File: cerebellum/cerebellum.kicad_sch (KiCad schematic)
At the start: 25 parts, among them J1 GPIO, J2 Conn_MOTA, J3 Conn_MOTB, J4 MD_POW, J5 Conn_SPI, J6 Conn_UART, J7 Conn_I2C, J8 VBUS(OUT), J9 3V3(OUT), SW1 SW_PULLUP, SW2 SW_PULLDOWN, SW3 SW_SPDT, U2 POLOLU_TB6612_CARRIER, U3 HC-SR04

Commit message: update design
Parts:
- SW1: value SW_PULLUP -> PULLUP
- SW2: value SW_PULLDOWN -> PULLDOWN
- SW3: footprint Button_Switch_THT:SW_E-Switch_EG1271_SPDT -> Connector_PinHeader_2.54mm:PinHeader_1x03_P2.54mm_Vertical
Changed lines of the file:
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@@
 			)
 		)
-		(property "Value" "SW_PULLUP"
+		(property "Value" "PULLUP"
 			(at 93.218 129.54 0)
 			(effects
@@
 			)
 		)
-		(property "Value" "SW_PULLDOWN"
+		(property "Value" "PULLDOWN"
 			(at 119.888 120.65 0)
 			(effects
@@
 			)
 		)
-		(property "Footprint" "Button_Switch_THT:SW_E-Switch_EG1271_SPDT"
+		(property "Footprint" "Connector_PinHeader_2.54mm:PinHeader_1x03_P2.54mm_Vertical"
 			(at 106.68 29.21 0)
 			(effects

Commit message: organize schematic
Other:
- note added: "Motor Driver"
- note added: "Pico & Peripherals"
- note added: "Pin Headers"
- title: RPi Expansion for Pico and Motor Driver (The Cerebellum) -> R1R Cerebellum
- moved on the sheet: A1, C2, C3, D1, J1, J2, J3, J4, J5, J6, J7, J8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

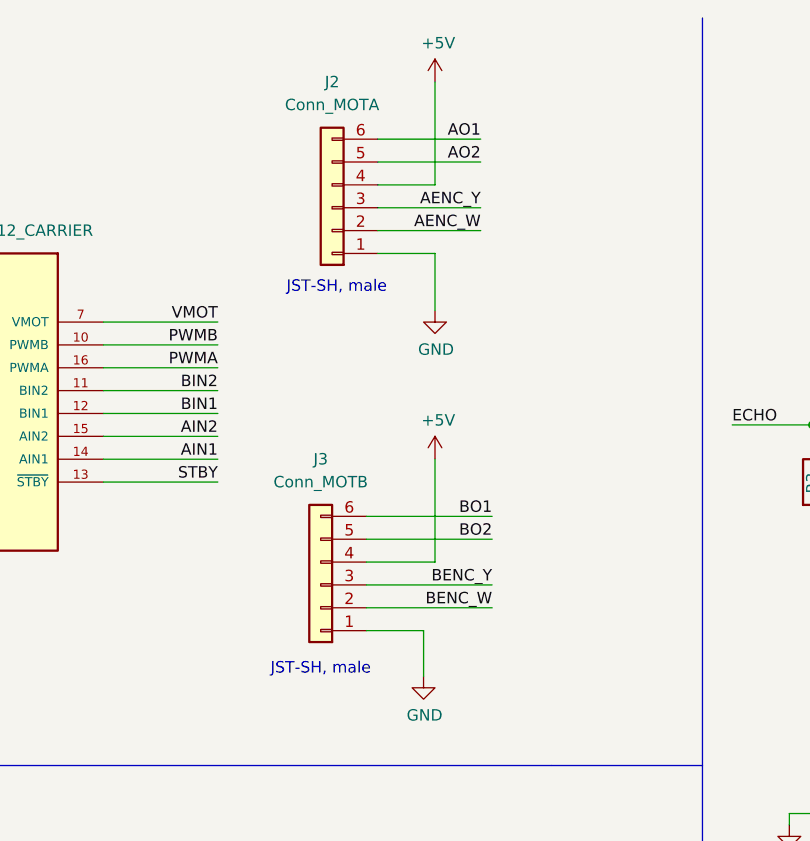
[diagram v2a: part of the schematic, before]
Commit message: update motor connector in schematic
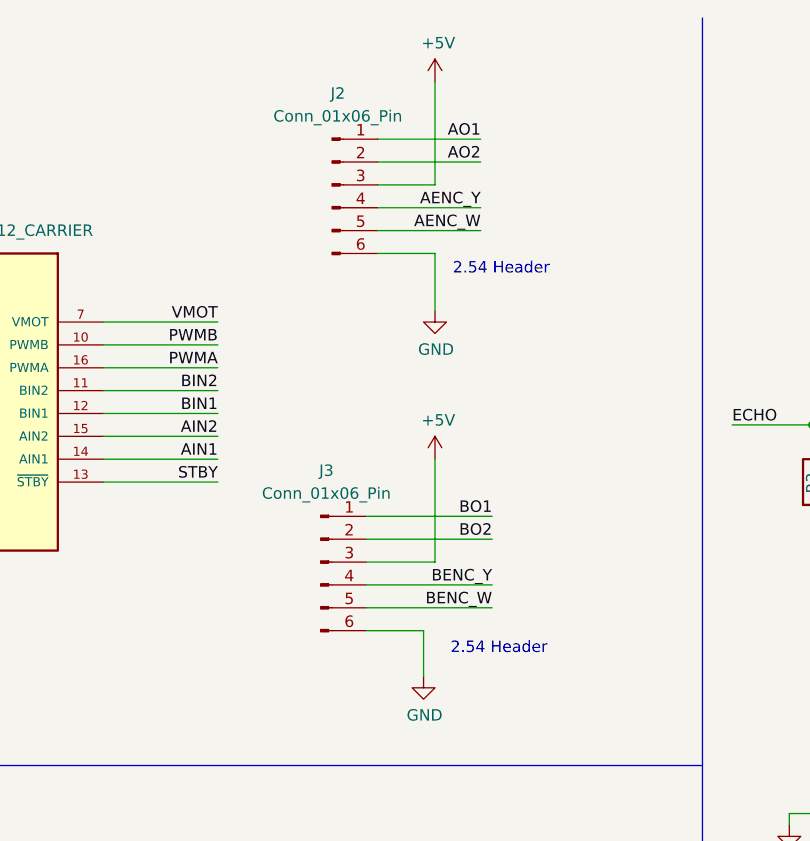
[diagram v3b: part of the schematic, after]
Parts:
- removed J2: Conn_MOTA, Connector_JST:JST_SH_BM06B-SRSS-TB_1x06-1MP_P1.00mm_Vertical, symbol Connector_Generic:Conn_01x06
- removed J3: Conn_MOTB, Connector_JST:JST_SH_BM06B-SRSS-TB_1x06-1MP_P1.00mm_Vertical, symbol Connector_Generic:Conn_01x06
- added J2, J3: Conn_01x06_Pin, Connector_PinHeader_2.54mm:PinHeader_1x06_P2.54mm_Vertical, symbol Connector:Conn_01x06_Pin
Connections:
- net +5V: now also J2.3 (Pin_3), J3.3 (Pin_3)
- net AENC_W: now also J2.5 (Pin_5)
- net AENC_Y: now also J2.4 (Pin_4)
- net AO1: now also J2.1 (Pin_1)
- net AO2: now also J2.2 (Pin_2)
- net BENC_W: now also J3.5 (Pin_5)
- net BENC_Y: now also J3.4 (Pin_4)
- net BO1: now also J3.1 (Pin_1)
- net BO2: now also J3.2 (Pin_2)
- net GND: now also J2.6 (Pin_6), J3.6 (Pin_6)
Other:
- note removed: "JST-SH, male"
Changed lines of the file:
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@@
 		(rev "0.1")
 	)
-	(text "JST-SH, male"
+	(text "2.54 Header"
 		(exclude_from_sim no)
-		(at 90.678 41.91 0)
+		(at 108.712 82.042 0)
 		(effects
 			(font
@@
 		)
 	)
+	(text "2.54 Header"
+		(exclude_from_sim no)
+		(at 108.966 39.878 0)
+		(effects
+			(font
+				(size 1.27 1.27)
+			)
+		)
+	)
 	(text "Additional pin functions:\nhttps://pinout.xyz/"
 		(exclude_from_sim no)
@@
 		)
 	)
-	(text "JST-SH, male"
-		(exclude_from_sim no)
-		(at 88.9 84.328 0)
-		(effects
-			(font
-				(size 1.27 1.27)
-			)
-		)
-	)
 	(text "Motor Driver"
 		(exclude_from_sim no)
@@
 	)
 	(symbol
-		(lib_id "Connector_Generic:Conn_01x06")
-		(at 88.9 74.93 180)
+		(lib_id "Connector_Generic:Conn_01x02")
+		(at 30.48 17.78 0)
 		(unit 1)
 		(exclude_from_sim no)
@@
 		(dnp no)
 		(fields_autoplaced yes)
-		(property "Reference" "J3"
-			(at 88.9 60.96 0)
+		(property "Reference" "J4"
+			(at 33.02 17.7799 0)
 			(effects
 				(font
 					(size 1.27 1.27)
 				)
+				(justify left)
 			)
 		)
-		(property "Value" "Conn_MOTB"
-			(at 88.9 63.5 0)
+		(property "Value" "MD_POW"
+			(at 33.02 20.3199 0)
 			(effects
 				(font
 					(size 1.27 1.27)
 				)
+				(justify left)
 			)
 		)
-		(property "Footprint" "Connector_JST:JST_SH_BM06B-SRSS-TB_1x06-1MP_P1.00mm_Vertical"
-			(at 88.9 74.93 0)
+		(property "Footprint" "Connector_PinHeader_2.54mm:PinHeader_1x02_P2.54mm_Horizontal"
+			(at 30.48 17.78 0)
 			(effects
 				(font
@@
 		)
 		(property "Datasheet" "~"
-			(at 88.9 74.93 0)
+			(at 30.48 17.78 0)
 			(effects
 				(font
@@
 			)
 		)
-		(property "Description" "Generic connector, single row, 01x06, script generated (kicad-library-utils/schlib/autogen/connector/)"
-			(at 88.9 74.93 0)
+		(property "Description" "Generic connector, single row, 01x02, script generated (kicad-library-utils/schlib/autogen/connector/)"
+			(at 30.48 17.78 0)
 			(effects
 				(font
@@
 			)
 		)
-		(pin "1"
-		)
-		(pin "4"
-		)
 		(pin "2"
 		)
-		(pin "3"
-		)
-		(pin "6"
-		)
-		(pin "5"
+		(pin "1"
 		)
 		(instances
 			(project ""
 				(path "/e63e39d7-6ac0-4ffd-8aa3-1841a4541b55"
-					(reference "J3")
+					(reference "J4")
 					(unit 1)
 				)
@@
 	)
 	(symbol
-		(lib_id "Connector_Generic:Conn_01x02")
-		(at 30.48 17.78 0)
+		(lib_id "Device:R")
+		(at 165.1 95.25 90)
 		(unit 1)
 		(exclude_from_sim no)
@@
 		(on_board yes)
 		(dnp no)
-		(fields_autoplaced yes)
-		(property "Reference" "J4"
-			(at 33.02 17.7799 0)
+		(property "Reference" "R5"
+			(at 165.1 95.25 90)
 			(effects
 				(font
 					(size 1.27 1.27)
 				)
-				(justify left)
 			)
 		)
-		(property "Value" "MD_POW"
-			(at 33.02 20.3199 0)
+		(property "Value" "220R"
+			(at 165.1 97.282 90)
 			(effects
 				(font
 					(size 1.27 1.27)
 				)
-				(justify left)
 			)
 		)
-		(property "Footprint" "Connector_PinHeader_2.54mm:PinHeader_1x02_P2.54mm_Horizontal"
-			(at 30.48 17.78 0)
+		(property "Footprint" "Resistor_THT:R_Axial_DIN0207_L6.3mm_D2.5mm_P10.16mm_Horizontal"
+			(at 165.1 97.028 90)
 			(effects
 				(font
@@
 		)
 		(property "Datasheet" "~"
-			(at 30.48 17.78 0)
+			(at 165.1 95.25 0)
 			(effects
 				(font
@@
 			)
 		)
-		(property "Description" "Generic connector, single row, 01x02, script generated (kicad-library-utils/schlib/autogen/connector/)"
-			(at 30.48 17.78 0)
+		(property "Description" "Resistor"
+			(at 165.1 95.25 0)
 			(effects
 				(font
@@
 			(project ""
 				(path "/e63e39d7-6ac0-4ffd-8aa3-1841a4541b55"
-					(reference "J4")
+					(reference "R5")
 					(unit 1)
 				)
@@
 	)
 	(symbol
-		(lib_id "Device:R")
-		(at 165.1 95.25 90)
+		(lib_id "Connector:Conn_01x06_Pin")
+		(at 90.17 30.48 0)
 		(unit 1)
 		(exclude_from_sim no)
@@
 		(on_board yes)
 		(dnp no)
-		(property "Reference" "R5"
-			(at 165.1 95.25 90)
+		(fields_autoplaced yes)
+		(property "Reference" "J2"
+			(at 90.805 20.32 0)
 			(effects
 				(font
@@
 			)
 		)
-		(property "Value" "220R"
-			(at 165.1 97.282 90)
+		(property "Value" "Conn_01x06_Pin"
+			(at 90.805 22.86 0)
 			(effects
 				(font
@@
 			)
 		)
-		(property "Footprint" "Resistor_THT:R_Axial_DIN0207_L6.3mm_D2.5mm_P10.16mm_Horizontal"
-			(at 165.1 97.028 90)
+		(property "Footprint" "Connector_PinHeader_2.54mm:PinHeader_1x06_P2.54mm_Vertical"
+			(at 90.17 30.48 0)
 			(effects
 				(font
@@
 		)
 		(property "Datasheet" "~"
-			(at 165.1 95.25 0)
+			(at 90.17 30.48 0)
 			(effects
 				(font
@@
 			)
 		)
-		(property "Description" "Resistor"
-			(at 165.1 95.25 0)
+		(property "Description" "Generic connector, single row, 01x06, script generated"
+			(at 90.17 30.48 0)
 			(effects
 				(font
@@
 			)
 		)
-		(pin "2"
+		(pin "5"
 		)
 		(pin "1"
 		)
+		(pin "6"
+		)
+		(pin "2"
+		)
+		(pin "4"
+		)
+		(pin "3"
+		)
 		(instances
 			(project ""
 				(path "/e63e39d7-6ac0-4ffd-8aa3-1841a4541b55"
-					(reference "R5")
+					(reference "J2")
 					(unit 1)
 				)
@@
 	)
 	(symbol
-		(lib_id "Connector_Generic:Conn_01x06")
-		(at 90.17 33.02 180)
+		(lib_id "Connector:Conn_01x06_Pin")
+		(at 88.9 72.39 0)
 		(unit 1)
 		(exclude_from_sim no)
@@
 		(dnp no)
 		(fields_autoplaced yes)
-		(property "Reference" "J2"
-			(at 90.17 19.05 0)
+		(property "Reference" "J3"
+			(at 89.535 62.23 0)
 			(effects
 				(font
@@
 			)
 		)
-		(property "Value" "Conn_MOTA"
-			(at 90.17 21.59 0)
+		(property "Value" "Conn_01x06_Pin"
+			(at 89.535 64.77 0)
 			(effects
 				(font
@@
 			)
 		)
-		(property "Footprint" "Connector_JST:JST_SH_BM06B-SRSS-TB_1x06-1MP_P1.00mm_Vertical"
-			(at 90.17 33.02 0)
+		(property "Footprint" "Connector_PinHeader_2.54mm:PinHeader_1x06_P2.54mm_Vertical"
+			(at 88.9 72.39 0)
 			(effects
 				(font
@@
 		)
 		(property "Datasheet" "~"
-			(at 90.17 33.02 0)
+			(at 88.9 72.39 0)
 			(effects
 				(font
@@
 			)
 		)
-		(property "Description" "Generic connector, single row, 01x06, script generated (kicad-library-utils/schlib/autogen/connector/)"
-			(at 90.17 33.02 0)
+		(property "Description" "Generic connector, single row, 01x06, script generated"
+			(at 88.9 72.39 0)
 			(effects
 				(font
@@
 			)
 		)
-		(pin "1"
+		(pin "2"
 		)
-		(pin "3"
+		(pin "1"
 		)
-		(pin "4"
+		(pin "6"
 		)
 		(pin "5"
 		)
-		(pin "6"
+		(pin "4"
 		)
-		(pin "2"
+		(pin "3"
 		)
 		(instances
 			(project ""
 				(path "/e63e39d7-6ac0-4ffd-8aa3-1841a4541b55"
-					(reference "J2")
+					(reference "J3")
 					(unit 1)
 				)

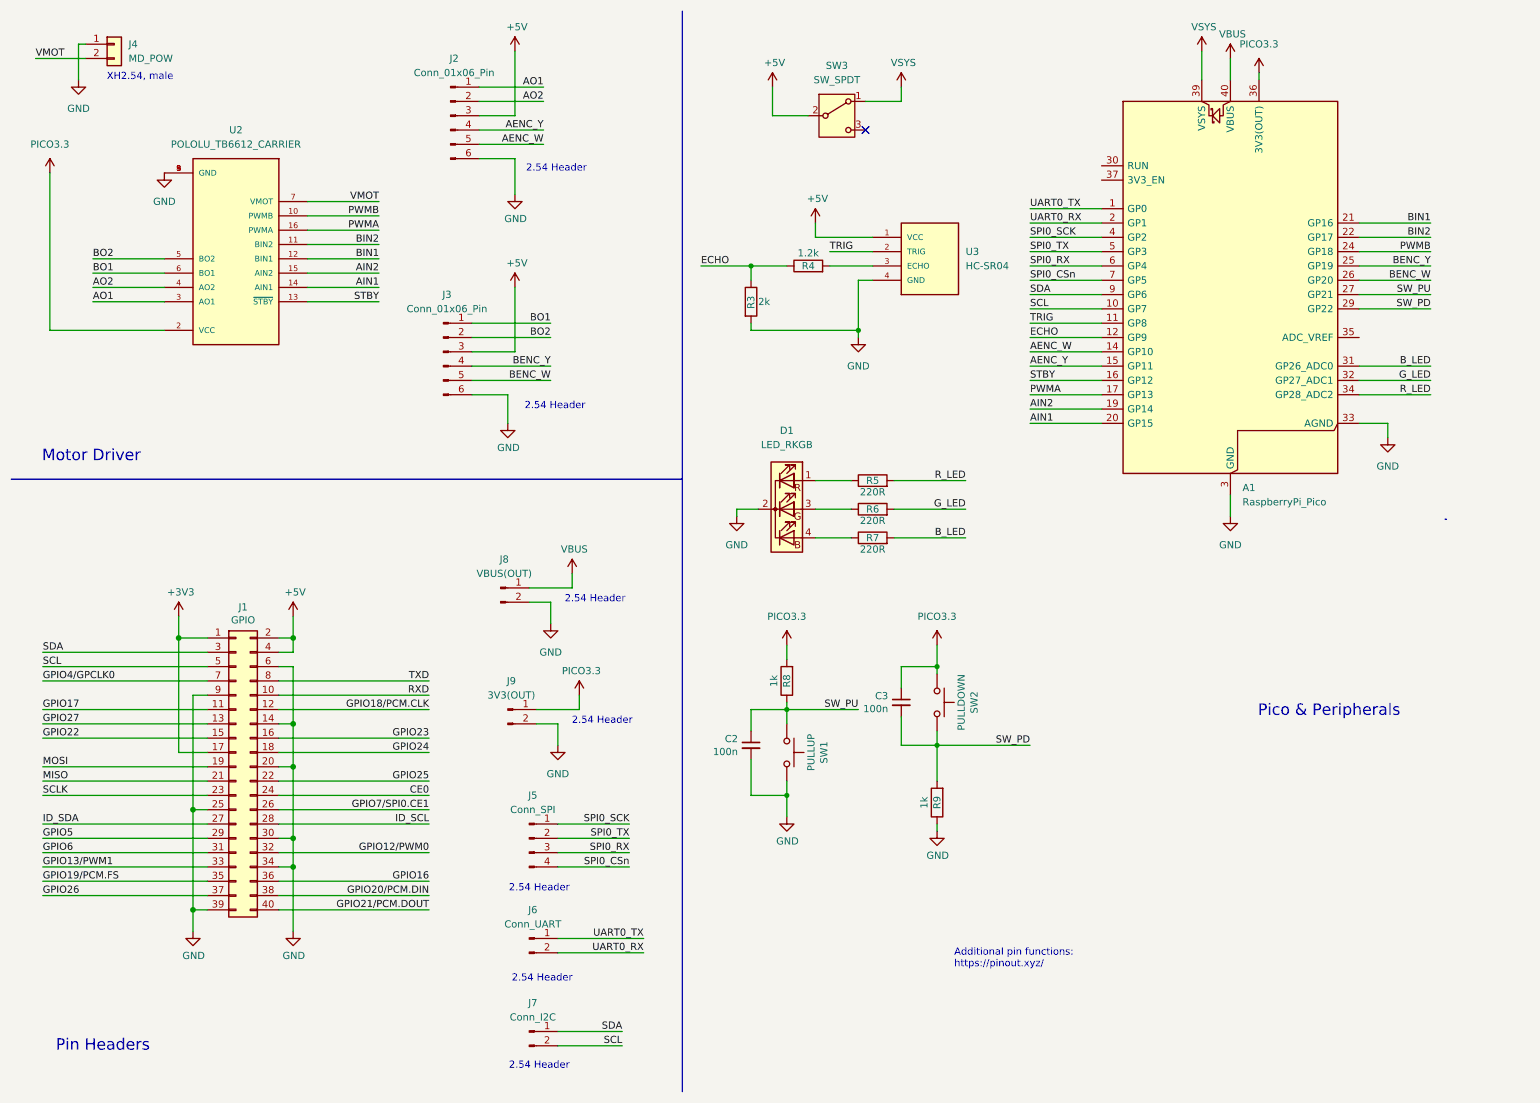
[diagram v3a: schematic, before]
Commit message: update symbol and footprint
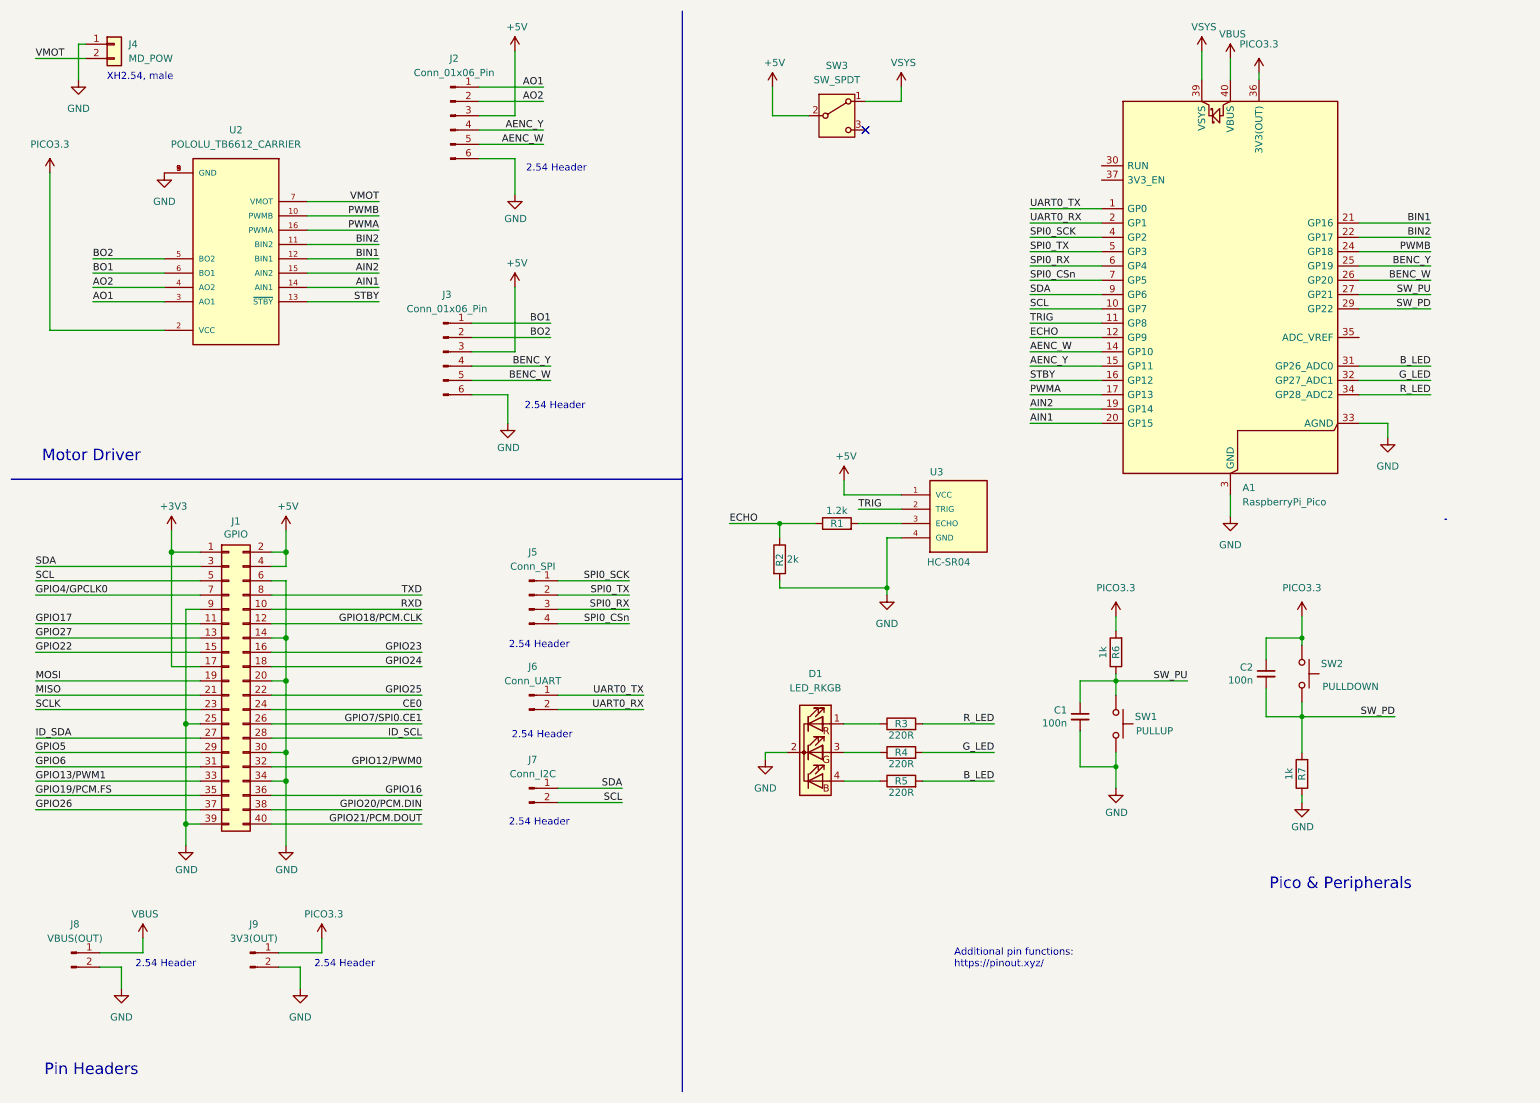
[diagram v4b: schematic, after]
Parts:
- renumbered C2 to C1, C3 to C2, R4 to R1, R3 to R2, R5 to R3, R6 to R4, R7 to R5, R8 to R6, R9 to R7
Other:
- moved on the sheet: C1, C2, D1, J1, J5, J6, J7, J8, J9, R1, R2, R3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

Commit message: update resistors and capacitors footprint to tht
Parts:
- C1, C2: footprint Capacitor_SMD:C_0805_2012Metric_Pad1.18x1.45mm_HandSolder -> Capacitor_THT:C_Disc_D4.7mm_W2.5mm_P5.00mm
- R1, R2, R6, R7: footprint Resistor_SMD:R_1206_3216Metric_Pad1.30x1.75mm_HandSolder -> Resistor_THT:R_Axial_DIN0207_L6.3mm_D2.5mm_P10.16mm_Horizontal
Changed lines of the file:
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@@
 			)
 		)
-		(property "Footprint" "Resistor_SMD:R_1206_3216Metric_Pad1.30x1.75mm_HandSolder"
+		(property "Footprint" "Resistor_THT:R_Axial_DIN0207_L6.3mm_D2.5mm_P10.16mm_Horizontal"
 			(at 158.75 104.648 90)
 			(effects
@@
 			)
 		)
-		(property "Footprint" "Capacitor_SMD:C_0805_2012Metric_Pad1.18x1.45mm_HandSolder"
+		(property "Footprint" "Capacitor_THT:C_Disc_D4.7mm_W2.5mm_P5.00mm"
 			(at 234.95 129.54 0)
 			(effects
@@
 			)
 		)
-		(property "Footprint" "Capacitor_SMD:C_0805_2012Metric_Pad1.18x1.45mm_HandSolder"
+		(property "Footprint" "Capacitor_THT:C_Disc_D4.7mm_W2.5mm_P5.00mm"
 			(at 201.93 137.16 0)
 			(effects
@@
 			)
 		)
-		(property "Footprint" "Resistor_SMD:R_1206_3216Metric_Pad1.30x1.75mm_HandSolder"
+		(property "Footprint" "Resistor_THT:R_Axial_DIN0207_L6.3mm_D2.5mm_P10.16mm_Horizontal"
 			(at 243.078 147.32 90)
 			(effects
@@
 			)
 		)
-		(property "Footprint" "Resistor_SMD:R_1206_3216Metric_Pad1.30x1.75mm_HandSolder"
+		(property "Footprint" "Resistor_THT:R_Axial_DIN0207_L6.3mm_D2.5mm_P10.16mm_Horizontal"
 			(at 146.812 109.22 90)
 			(effects
@@
 			)
 		)
-		(property "Footprint" "Resistor_SMD:R_1206_3216Metric_Pad1.30x1.75mm_HandSolder"
+		(property "Footprint" "Resistor_THT:R_Axial_DIN0207_L6.3mm_D2.5mm_P10.16mm_Horizontal"
 			(at 210.058 125.73 90)
 			(effects

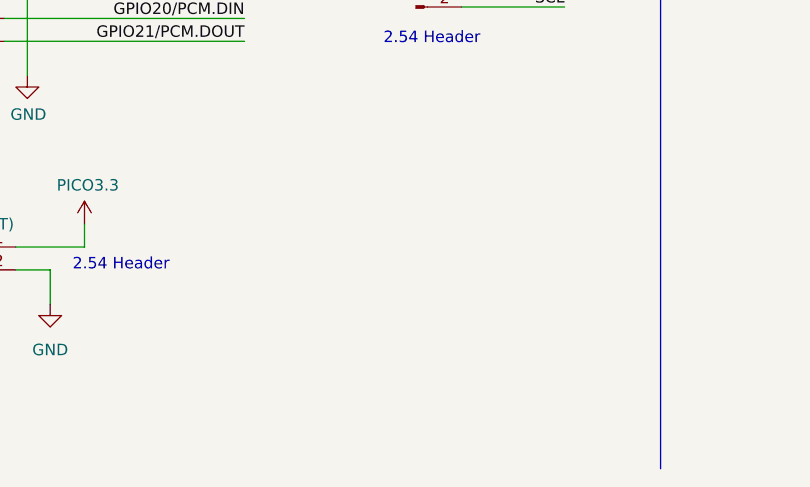
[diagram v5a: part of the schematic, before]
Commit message: update pico power outlet pins footprint
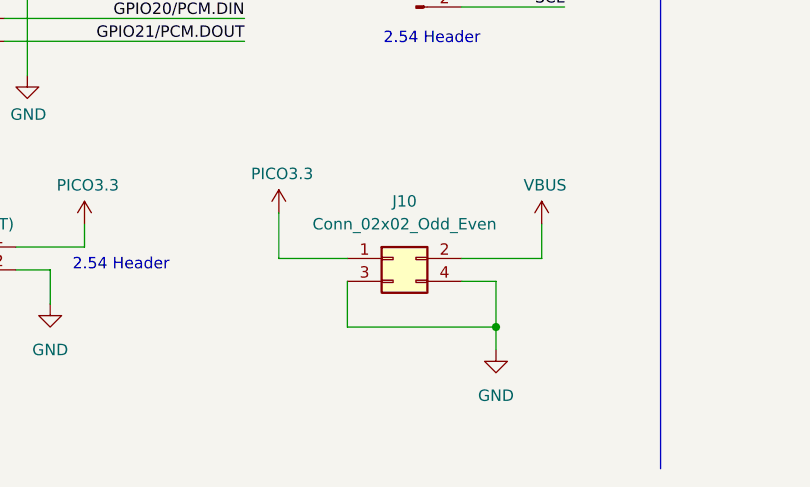
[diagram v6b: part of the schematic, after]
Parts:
- added J10: Conn_02x02_Odd_Even, Connector_PinHeader_2.54mm:PinHeader_2x02_P2.54mm_Vertical, symbol Connector_Generic:Conn_02x02_Odd_Even
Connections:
- net GND: now also J10.3 (Pin_3), J10.4 (Pin_4)
- net PICO3.3: now also J10.1 (Pin_1)
- net VBUS: now also J10.2 (Pin_2)

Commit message: save schematic change, minor
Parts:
- removed J8: VBUS(OUT), Connector_PinHeader_2.54mm:PinHeader_1x02_P2.54mm_Vertical, symbol Connector:Conn_01x02_Pin
- removed J9: 3V3(OUT), Connector_PinHeader_2.54mm:PinHeader_1x02_P2.54mm_Vertical, symbol Connector:Conn_01x02_Pin
- renumbered J10 to J8
